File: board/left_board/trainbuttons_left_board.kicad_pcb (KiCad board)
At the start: 4 copper layers, 302.5 x 95 mm, 55 parts, among them J101 USB_C_Receptacle_USB2.0_16P, J102 HDMI_A, J301 HDMI_A, J401 UART, J801 DBG, SW201 SW_Push, SW202 SW_Push, SW203 SW_Push, SW204 SW_Push, SW205 SW_Push, SW206 SW_Push, SW207 SW_Push, SW208 SW_Push, SW209 SW_Push, SW210 SW_Push, SW211 SW_Push, SW212 SW_Push, SW213 SW_Push, SW301 SW_Push, SW302 SW_Push, SW303 SW_Push, SW304 SW_Push, SW305 SW_Push, SW306 SW_Push, SW307 SW_Push, SW308 SW_Push, SW801 RST, U401 STM32G0B0CETx, U501 LM317AEMP, Y601 48MHz

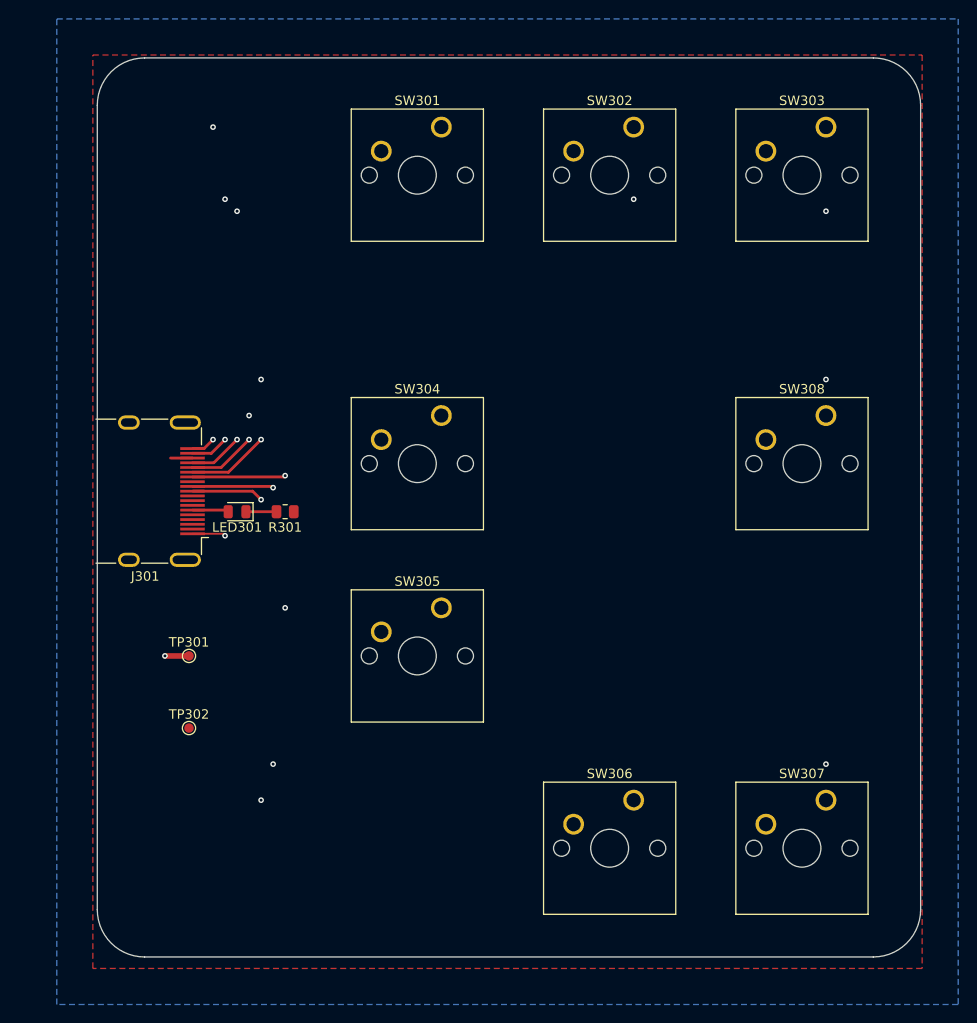
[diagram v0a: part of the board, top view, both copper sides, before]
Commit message: split board into left and right
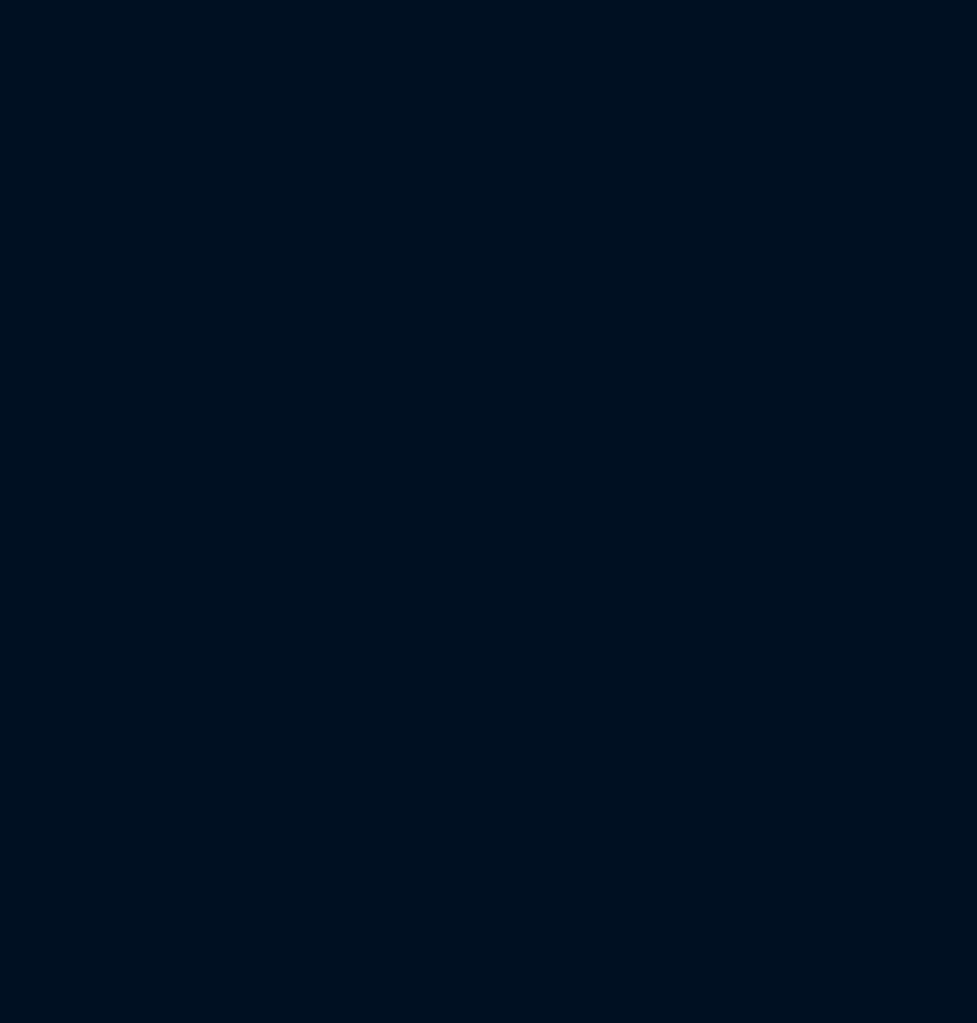
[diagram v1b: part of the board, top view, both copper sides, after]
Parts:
- removed J301: HDMI_A, Connector_HDMI:HDMI_A_Molex_208658-1001_Horizontal
- removed LED301: LED, LED_SMD:LED_0805_2012Metric
- removed R301: 68Ω, Resistor_SMD:R_0805_2012Metric
- removed SW301, SW302, SW303, SW304, SW305, SW306, SW307, SW308: SW_Push, Button_Switch_Keyboard:SW_Cherry_MX_1.00u_PCB
- removed TP301, TP302: TestPoint, TestPoint:TestPoint_Pad_D1.0mm
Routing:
- net /Right Buttons/HEADLIGHT: track 101.0 -> 0.00 mm, vias 3 -> 0
- net /Right Buttons/BELL: track 100.0 -> 0.00 mm, vias 3 -> 0
- net /Right Buttons/BRAKE_RLS: track 80.3 -> 0.00 mm, vias 3 -> 0
- net /Right Buttons/HORN: track 78.7 -> 0.00 mm, vias 2 -> 0
- net /Right Buttons/BRAKE_SCHG: track 78.5 -> 0.00 mm, vias 3 -> 0
- net /Right Buttons/SAND: track 59.7 -> 0.00 mm, vias 2 -> 0
- net /Right Buttons/TDIR_DN: track 40.3 -> 0.00 mm, vias 2 -> 0
- net /Right Buttons/TDIR_UP: track 30.1 -> 0.00 mm, vias 2 -> 0
- net /Right Buttons/+3.3V: track 6.07 -> 0.00 mm, vias 2 -> 0
- net /Right Buttons/RLED: track 3.60 -> 0.00 mm
- net Net-(LED301-K): track 3.23 -> 0.00 mm
- net /Right Buttons/GND: track 2.32 -> 0.00 mm
- removed copper zone on In1.Cu, net /Right Buttons/+3.3V
- removed copper zone on In2.Cu, net /Right Buttons/+3.3V
- removed copper zone on B.Cu, net /Right Buttons/GND
- removed copper zone on F.Cu, net /Right Buttons/GND
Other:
- board size 302.5 x 95 mm -> 182 x 73 mm

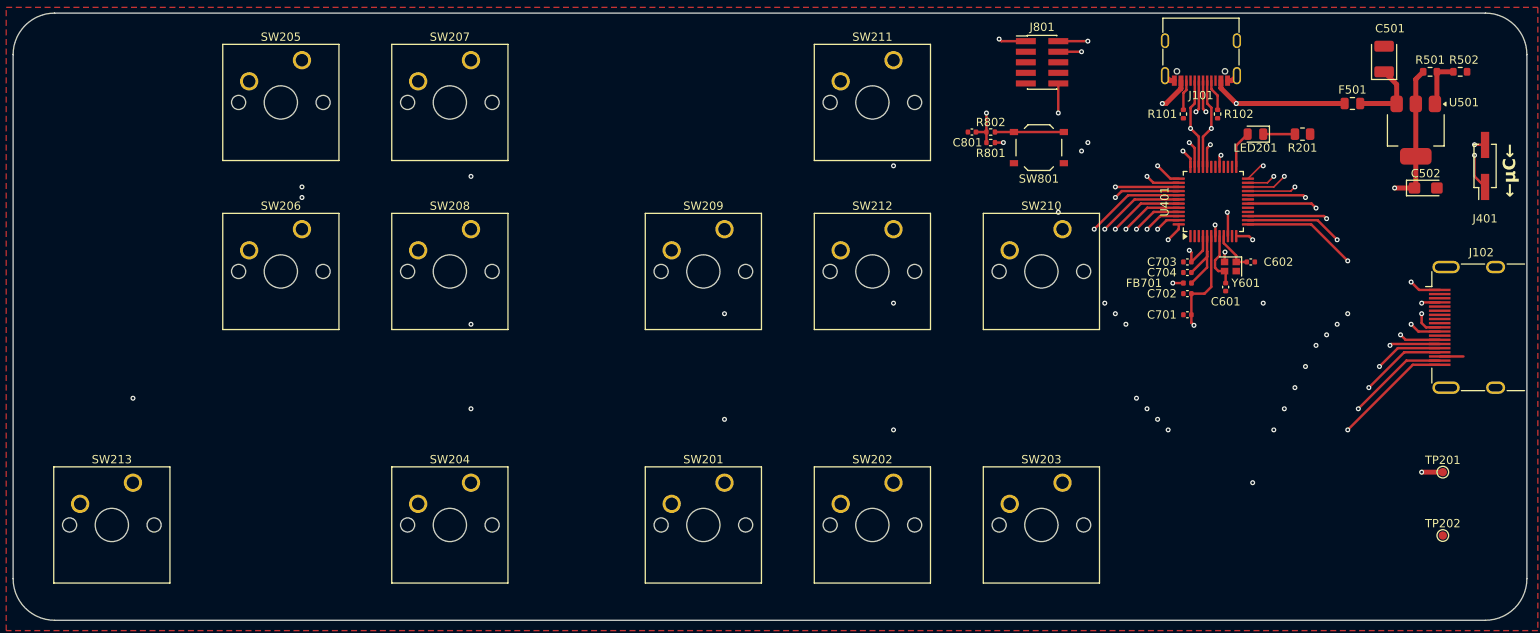
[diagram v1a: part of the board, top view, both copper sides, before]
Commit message: boards: add JLCPCB mounting holes
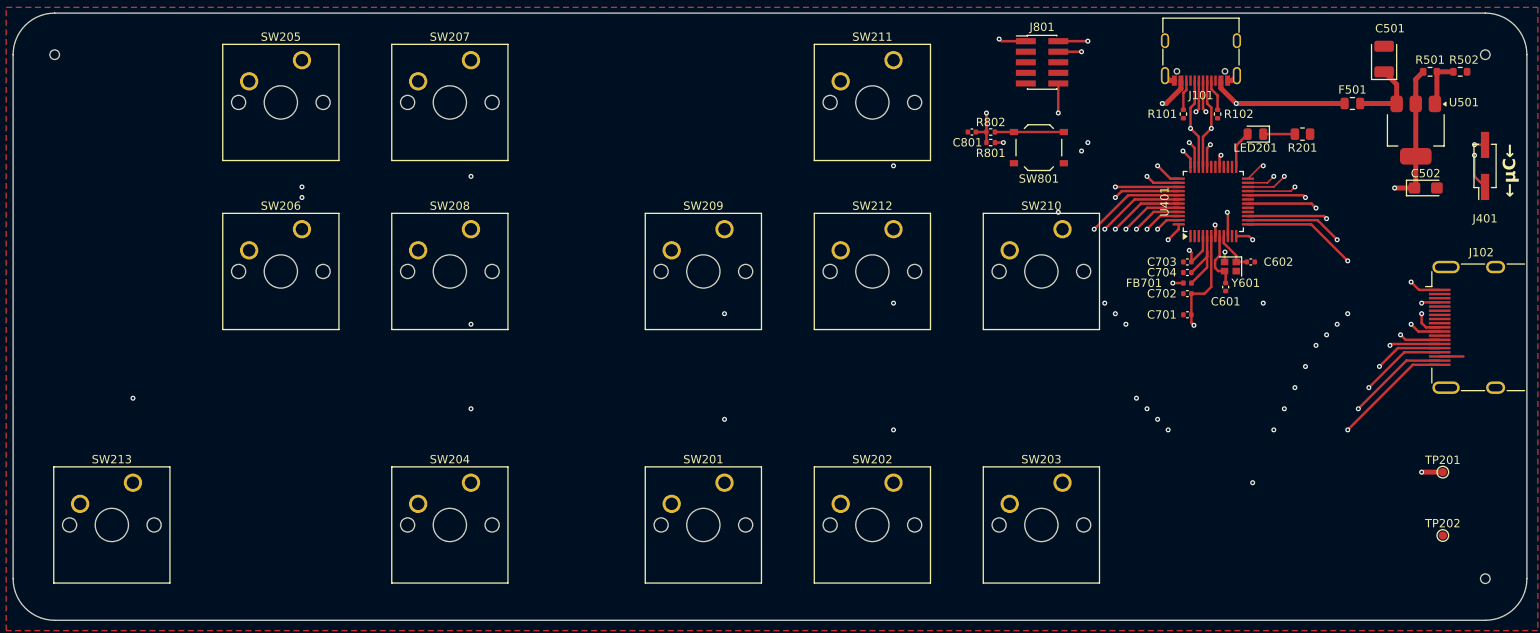
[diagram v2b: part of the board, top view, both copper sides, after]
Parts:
- added REF**: JLCPCB_Mounting_Hole, JLCPCB:JLCPCB_Mounting_Hole, F.Cu at (207.0, 104.2)
- added REF**: JLCPCB_Mounting_Hole, JLCPCB:JLCPCB_Mounting_Hole, F.Cu at (35.0, 41.2)
- added REF**: JLCPCB_Mounting_Hole, JLCPCB:JLCPCB_Mounting_Hole, F.Cu at (207.0, 41.2)
